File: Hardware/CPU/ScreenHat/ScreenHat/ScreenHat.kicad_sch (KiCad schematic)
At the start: 2 parts, among them U1 PCF8574AT, U2 LCD_20x4

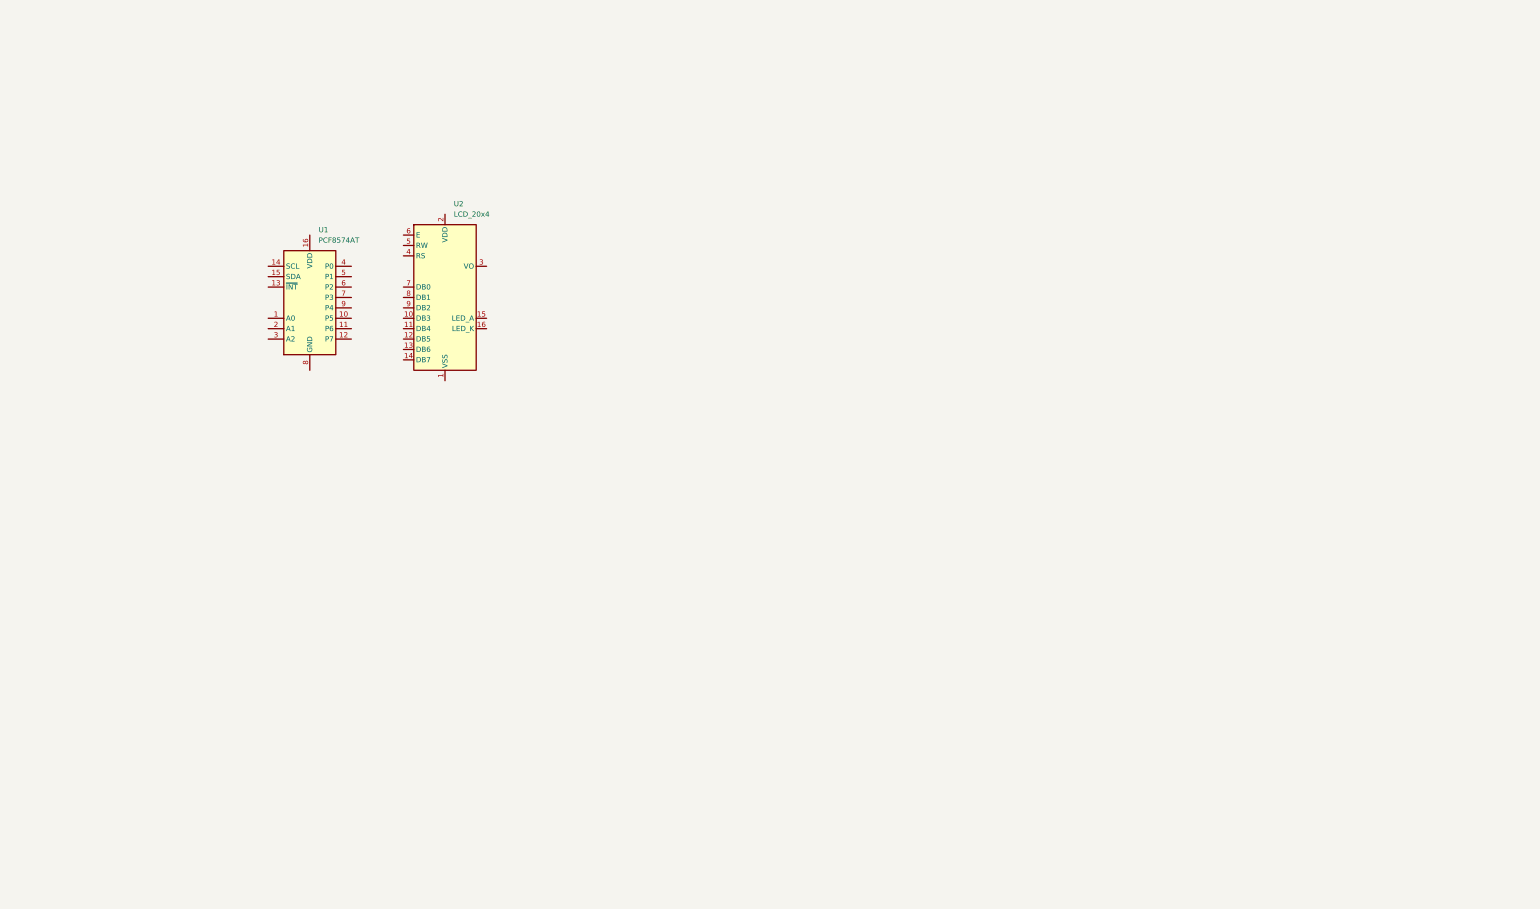
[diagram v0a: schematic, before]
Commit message: finished ScreenHat Schematics
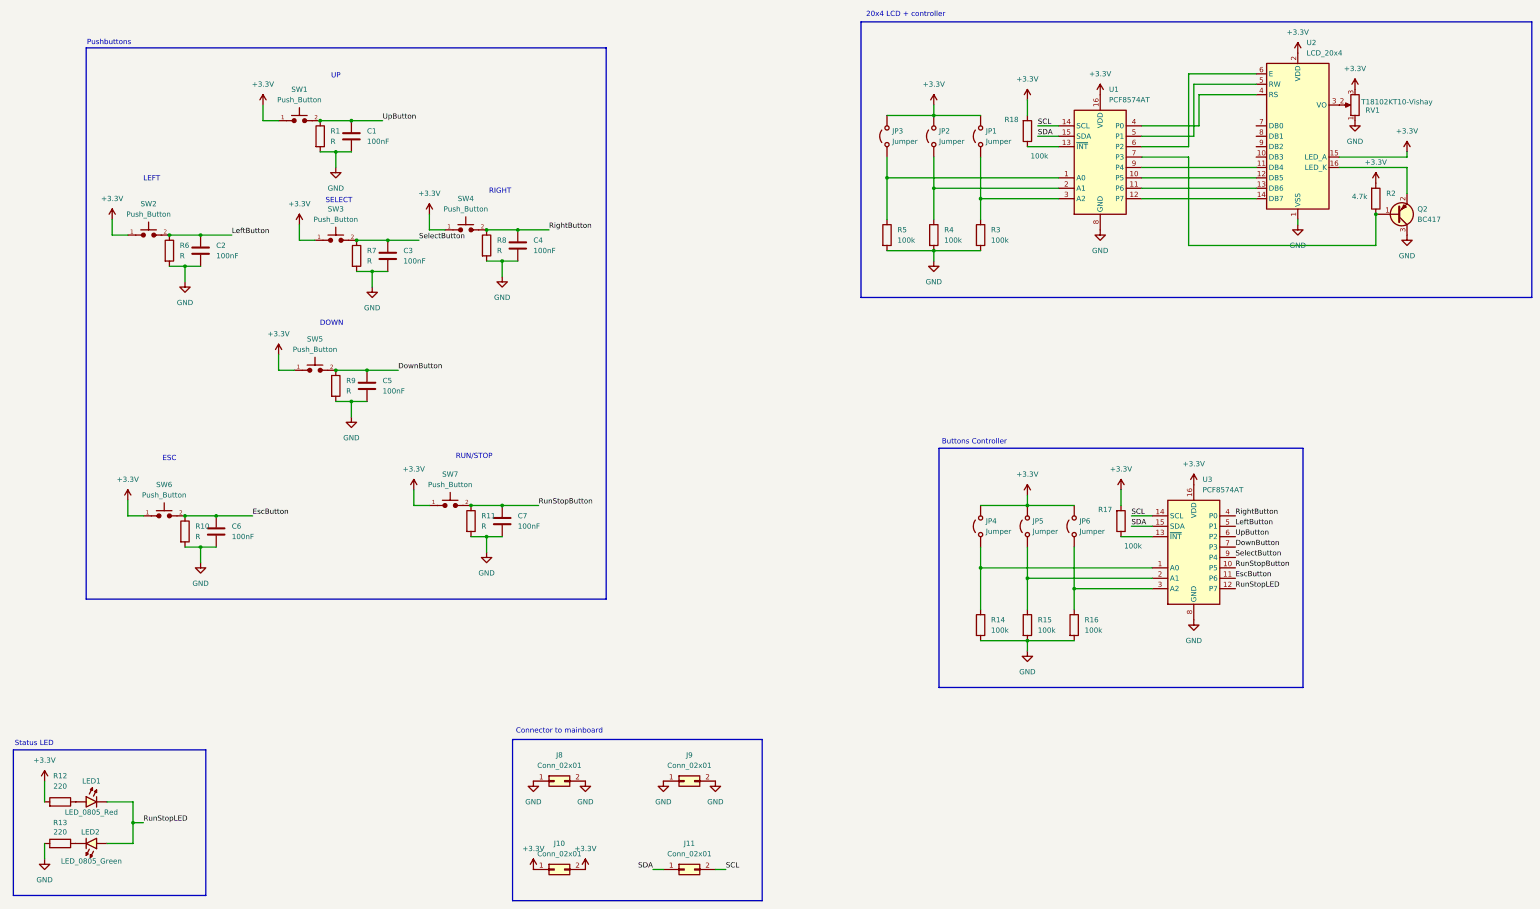
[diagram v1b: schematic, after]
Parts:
- added C1, C2, C3, C4, C5, C6, C7: 100nF, Capacitor_SMD:C_0805_2012Metric_Pad1.18x1.45mm_HandSolder, symbol PCM_Capacitor_AKL:C_0805
- added J10, J11, J8, J9: Conn_02x01, Connector_PinHeader_2.54mm:PinHeader_2x01_P2.54mm_Vertical, symbol Connector_Generic:Conn_02x01
- added JP1, JP2, JP3, JP4, JP5, JP6: Jumper, Jumper:SolderJumper-2_P1.3mm_Open_RoundedPad1.0x1.5mm, symbol Jumper:Jumper_2_Open
- added LED1: LED_0805_Red, PCM_LED_SMD_AKL:LED_0805_2012Metric, symbol PCM_LED_AKL:LED_0805_Red
- added LED2: LED_0805_Green, PCM_LED_SMD_AKL:LED_0805_2012Metric, symbol PCM_LED_AKL:LED_0805_Green
- added Q2: BC417, PCM_Package_TO_SOT_SMD_AKL:SOT-23, symbol PCM_Transistor_BJT_AKL:2SA2119K
- added R1, R10, R11, R6, R7, R8, R9: R, PCM_Resistor_SMD_AKL:R_0805_2012Metric_Pad1.15x1.40mm_HandSolder, symbol Device:R
- added R12, R13: 220, PCM_Resistor_SMD_AKL:R_0805_2012Metric, symbol PCM_Resistor_AKL:R_0805
- added R14, R15, R16, R3, R4, R5: 100k, PCM_Resistor_SMD_AKL:R_0805_2012Metric_Pad1.15x1.40mm_HandSolder, symbol Device:R
- added R17, R18: 100k, PCM_Resistor_SMD_AKL:R_0805_2012Metric, symbol PCM_Resistor_AKL:R_0805
- added R2: 4.7k, PCM_Resistor_SMD_AKL:R_0805_2012Metric, symbol PCM_Resistor_AKL:R_0805
- added RV1: T18102KT10-Vishay, PCM_Potentiometer_THT_AKL_Double:Potentiometer_Bourns_3009P_Horizontal, symbol Device:R_Potentiometer
- added SW1, SW2, SW3, SW4, SW5, SW6, SW7: Push_Button, Button_Switch_SMD:SW_SPST_Omron_B3FS-105xP, symbol PCM_SL_Devices:Push_Button
- added U3: PCF8574AT, Package_SO:SOIC-16W_7.5x10.3mm_P1.27mm, symbol Interface_Expansion:PCF8574AT
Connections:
- net GND: now reaches U2.1 (VSS)
- net GND: now also U1.8 (GND), C1.2, C2.2, C3.2, C4.2, C5.2, C6.2, C7.2, J8.1 (Pin_1), J8.2 (Pin_2), J9.1 (Pin_1), J9.2 (Pin_2), Q2.3 (C), R1.2, R10.2, R11.2, R13.1, R14.2, R15.2, R16.2, R3.2, R4.2, R5.2, R6.2, R7.2, R8.2, R9.2, RV1.1, U3.8 (GND)
- net at U2.11 (DB4): now also U1.9 (P4)
- net at U2.12 (DB5): now also U1.10 (P5)
- net at U2.13 (DB6): now also U1.11 (P6)
- net at U2.14 (DB7): now also U1.12 (P7)
- net +3.3V: now reaches U2.15 (LED_A)
- net +3.3V: now also U1.16 (VDD), U2.2 (VDD), J10.1 (Pin_1), J10.2 (Pin_2), JP1.2 (B), JP2.2 (B), JP3.2 (B), JP4.2 (B), JP5.2 (B), JP6.2 (B), R12.1, R17.1, R18.1, R2.1, RV1.3, SW1.1, SW2.1, SW3.1, SW4.1, SW5.1, SW6.1, SW7.1, U3.16 (VDD)
- net at U2.16 (LED_K): now also Q2.2 (E)
- net at U2.3 (VO): now also RV1.2
- net at U2.4 (RS): now also U1.4 (P0)
- net at U2.5 (RW): now also U1.5 (P1)
- net at U2.6 (E): now also U1.6 (P2)
- net at U1.1 (A0): now also JP3.1 (A), R5.1
- net at U1.13 (~{INT}): now also R18.2
- net SCL: now reaches U1.14 (SCL)
- net SCL: now also J11.2 (Pin_2), U3.14 (SCL)
- net SDA: now reaches U1.15 (SDA)
- net SDA: now also J11.1 (Pin_1), U3.15 (SDA)
- net at U1.2 (A1): now also JP2.1 (A), R4.1
- net at U1.3 (A2): now also JP1.1 (A), R3.1
- net at U1.7 (P3): now also Q2.1 (B), R2.2
- new net: R17.2, U3.13 (~{INT})
- new net: JP6.1 (A), R16.1, U3.3 (A2)
- new net: LED1.2 (A), R12.2
- new net: JP4.1 (A), R14.1, U3.1 (A0)
- new net: JP5.1 (A), R15.1, U3.2 (A1)
- new net: LED2.1 (K), R13.2
- new net DownButton: C5.1, R9.1, SW5.2, U3.7 (P3)
- new net EscButton: C6.1, R10.1, SW6.2, U3.11 (P6)
- new net LeftButton: C2.1, R6.1, SW2.2, U3.5 (P1)
- new net RightButton: C4.1, R8.1, SW4.2, U3.4 (P0)
- new net RunStopButton: C7.1, R11.1, SW7.2, U3.10 (P5)
- new net RunStopLED: LED1.1 (K), LED2.2 (A), U3.12 (P7)
- new net SelectButton: C3.1, R7.1, SW3.2, U3.9 (P4)
- new net UpButton: C1.1, R1.1, SW1.2, U3.6 (P2)
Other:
- note added: "20x4 LCD + controller"
- note added: "Buttons Controller"
- note added: "Connector to mainboard"
- note added: "DOWN"
- note added: "ESC"
- note added: "LEFT"
- note added: "Pushbuttons"
- note added: "RIGHT"
- note added: "RUN/STOP"
- note added: "SELECT"
- note added: "Status LED"
- note added: "UP"
- moved on the sheet: U1, U2
